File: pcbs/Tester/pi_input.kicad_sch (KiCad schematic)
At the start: 3 parts, among them J201 Raspberry_Pi_2_3, U201 SN74LVC4245APWR, U202 SN74LVC4245APWR

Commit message: More renaming
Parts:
- added U?: SN74LVC4245APWR, Package_SO:TSSOP-24_4.4x7.8mm_P0.65mm, symbol LevelShifter:SN74LVC4245APWR
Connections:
- net +3V3: now also U?.23 (VCCB), U?.24 (VCCB)
- net +5V: now also U?.1 (VCCA)
- net GND: now also U?.11 (GND), U?.12 (GND), U?.13 (GND), U?.14 (B8), U?.18 (B4), U?.2 (DIR), U?.22 (~{OE}); no longer U201.14 (B8), U201.18 (B4)
- net IN_{CLK}: now also U?.9 (A7); no longer U201.9 (A7)
- net SPI1_{CLK}: now also U?.15 (B7); no longer U201.15 (B7)
- net ~{IN_{LOAD}}: now also U?.8 (A6); no longer U201.8 (A6)
- net ~{IN_{SELECT}}: now also U?.7 (A5); no longer U201.7 (A5)
- net ~{SPI1_{LOAD}}: now also U?.16 (B6); no longer U201.16 (B6)
- net ~{SPI1_{SELECT}}: now also U?.17 (B5); no longer U201.17 (B5)
- net ~{OE5}: now reaches U201.10 (A8)
- net ~{OE1}: now reaches U201.6 (A4)
- new net ~{OE2}: U201.7 (A5)
- new net ~{OE3}: U201.8 (A6)
- new net ~{OE4}: U201.9 (A7)
- new net ~{SPI0_{OE1}}: U201.14 (B8), U201.15 (B7), U201.16 (B6), U201.17 (B5), U201.18 (B4)
- no-connect marks 30 -> 13
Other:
- moved on the sheet: U201, U202

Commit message: Lots of rethinking
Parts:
- gave numbers to parts that had none: 1
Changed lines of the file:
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@@
   (symbol (lib_id "power:GND") (at 276.225 66.04 90) (unit 1)
     (in_bom yes) (on_board yes) (fields_autoplaced)
-    (property "Reference" "#PWR?" (id 0) (at 282.575 66.04 0)
+    (property "Reference" "#PWR0222" (id 0) (at 282.575 66.04 0)
       (effects (font (size 1.27 1.27)) hide)
     )
@@
   (symbol (lib_id "power:+5V") (at 227.965 38.1 90) (unit 1)
     (in_bom yes) (on_board yes) (fields_autoplaced)
-    (property "Reference" "#PWR?" (id 0) (at 231.775 38.1 0)
+    (property "Reference" "#PWR0218" (id 0) (at 231.775 38.1 0)
       (effects (font (size 1.27 1.27)) hide)
     )
@@
   (symbol (lib_id "power:+3V3") (at 263.525 39.37 270) (unit 1)
     (in_bom yes) (on_board yes) (fields_autoplaced)
-    (property "Reference" "#PWR?" (id 0) (at 259.715 39.37 0)
+    (property "Reference" "#PWR0220" (id 0) (at 259.715 39.37 0)
       (effects (font (size 1.27 1.27)) hide)
     )
@@
   (symbol (lib_id "power:GND") (at 276.225 55.88 90) (unit 1)
     (in_bom yes) (on_board yes) (fields_autoplaced)
-    (property "Reference" "#PWR?" (id 0) (at 282.575 55.88 0)
+    (property "Reference" "#PWR0221" (id 0) (at 282.575 55.88 0)
       (effects (font (size 1.27 1.27)) hide)
     )
@@
   (symbol (lib_id "power:GND") (at 227.965 41.91 270) (unit 1)
     (in_bom yes) (on_board yes) (fields_autoplaced)
-    (property "Reference" "#PWR?" (id 0) (at 221.615 41.91 0)
+    (property "Reference" "#PWR0219" (id 0) (at 221.615 41.91 0)
       (effects (font (size 1.27 1.27)) hide)
     )
@@
   (symbol (lib_id "LevelShifter:SN74LVC4245APWR") (at 245.745 57.15 0) (unit 1)
     (in_bom yes) (on_board yes)
-    (property "Reference" "U?" (id 0) (at 245.745 29.083 0))
+    (property "Reference" "U203" (id 0) (at 245.745 29.083 0))
     (property "Value" "SN74LVC4245APWR" (id 1) (at 245.745 31.3944 0))
     (property "Footprint" "Package_SO:TSSOP-24_4.4x7.8mm_P0.65mm" (id 2) (at 245.745 57.15 0)
@@
   (symbol (lib_id "power:GND") (at 219.075 44.45 270) (unit 1)
     (in_bom yes) (on_board yes) (fields_autoplaced)
-    (property "Reference" "#PWR?" (id 0) (at 212.725 44.45 0)
+    (property "Reference" "#PWR0216" (id 0) (at 212.725 44.45 0)
       (effects (font (size 1.27 1.27)) hide)
     )
@@
   (symbol (lib_id "power:GND") (at 226.695 74.93 270) (unit 1)
     (in_bom yes) (on_board yes) (fields_autoplaced)
-    (property "Reference" "#PWR?" (id 0) (at 220.345 74.93 0)
-      (effects (font (size 1.27 1.27)) hide)
-    )
+    (property "Reference" "#PWR0217" (id 0) (at 220.345 74.93 0)
+      (effects (font (size 1.27 1.27)) hide)
+    )

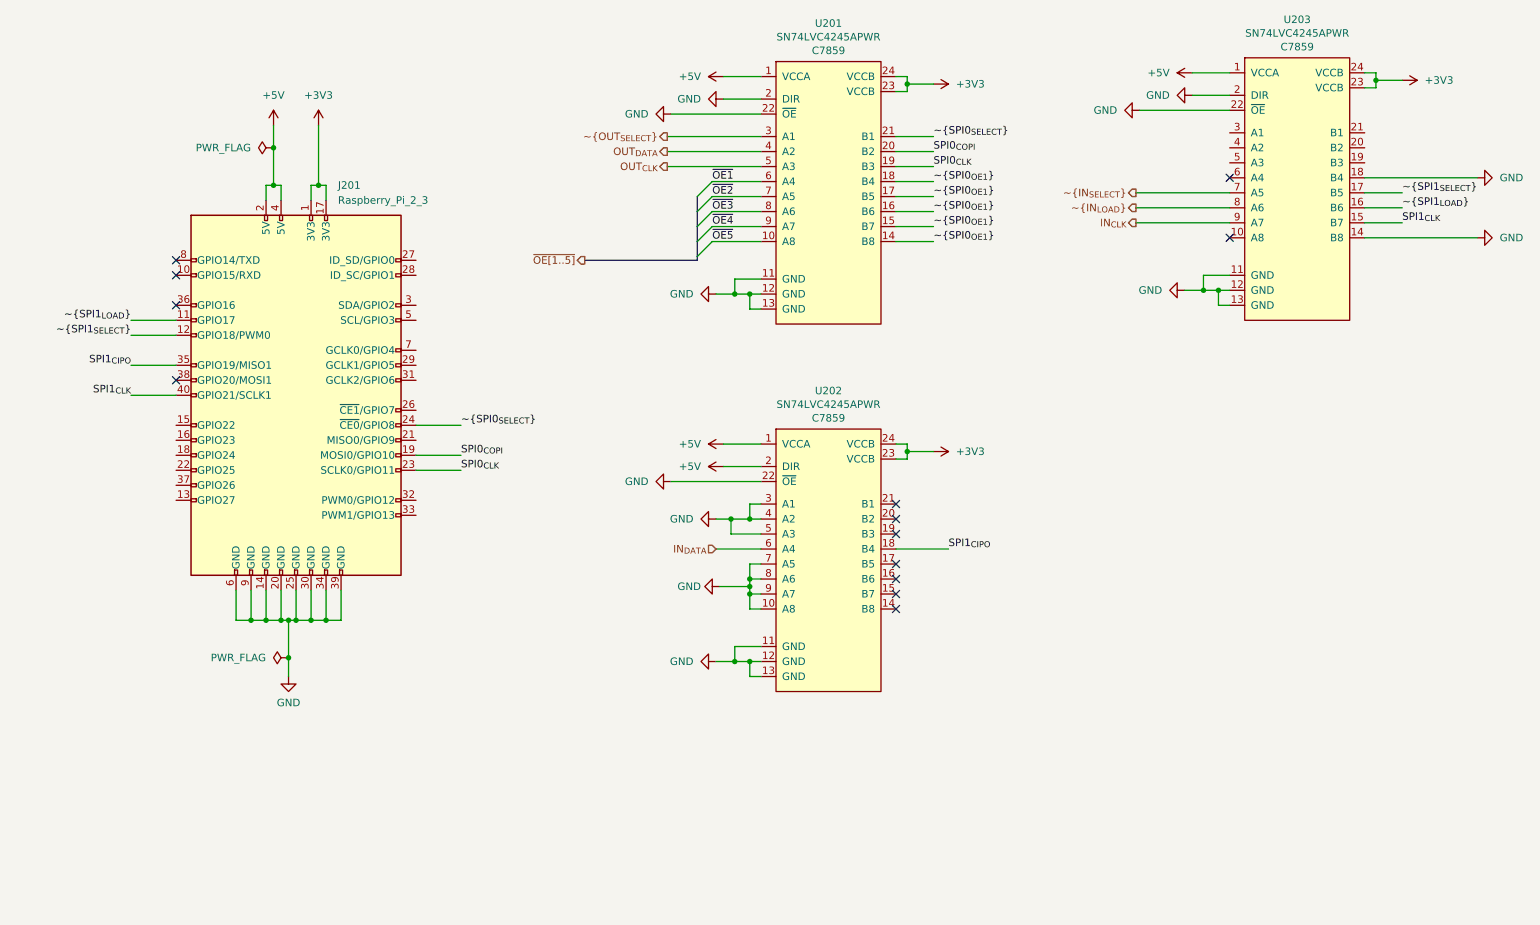
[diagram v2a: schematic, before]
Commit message: Shift register routing
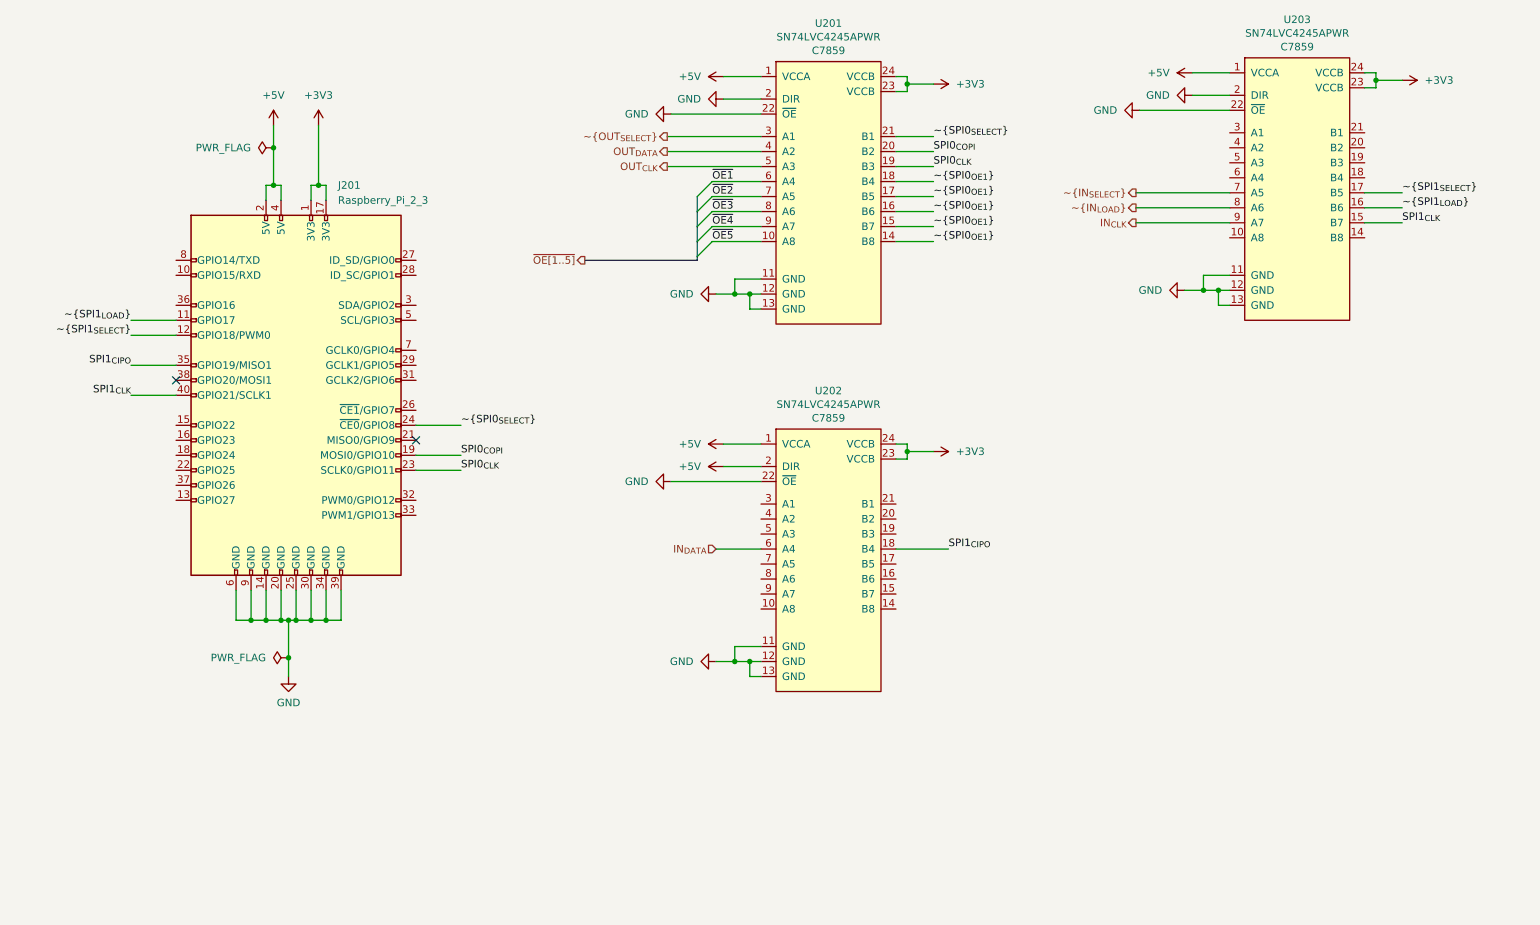
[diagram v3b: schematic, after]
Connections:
- net GND: no longer U202.10 (A8), U202.3 (A1), U202.4 (A2), U202.5 (A3), U202.7 (A5), U202.8 (A6), U202.9 (A7), U203.14 (B8), U203.18 (B4)
- no-connect marks 13 -> 2
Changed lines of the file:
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@@
   (junction (at 72.39 57.15) (diameter 0) (color 0 0 0 0)
   )
-  (junction (at 153.035 123.825) (diameter 0) (color 0 0 0 0)
-  )
   (junction (at 78.74 130.81) (diameter 0) (color 0 0 0 0)
   )
-  (junction (at 153.035 126.365) (diameter 0) (color 0 0 0 0)
-  )
   (junction (at 68.58 130.81) (diameter 0) (color 0 0 0 0)
   )
@@
   (junction (at 76.2 130.81) (diameter 0) (color 0 0 0 0)
   )
-  (junction (at 149.86 113.665) (diameter 0) (color 0 0 0 0)
-  )
-  (junction (at 153.035 125.095) (diameter 0) (color 0 0 0 0)
-  )
-  (junction (at 153.035 113.665) (diameter 0) (color 0 0 0 0)
-  )
   (junction (at 81.28 130.81) (diameter 0) (color 0 0 0 0)
   )
   (junction (at 179.705 102.235) (diameter 0) (color 0 0 0 0)
   )
-  (no_connect (at 177.8 126.365))
-  (no_connect (at 177.8 111.125))
-  (no_connect (at 177.8 123.825))
-  (no_connect (at 234.315 66.04))
-  (no_connect (at 177.8 113.665))
-  (no_connect (at 177.8 128.905))
-  (no_connect (at 177.8 121.285))
-  (no_connect (at 55.88 77.47))
+  (no_connect (at 96.52 100.33))
   (no_connect (at 55.88 90.17))
-  (no_connect (at 55.88 69.85))
-  (no_connect (at 55.88 72.39))
-  (no_connect (at 177.8 116.205))
-  (no_connect (at 234.315 55.88))
   (bus_entry (at 144.145 61.595) (size 2.54 -2.54)
     (stroke (width 0) (type default) (color 0 0 0 0))
@@
     (stroke (width 0) (type default) (color 0 0 0 0))
   )
-  (wire (pts (xy 154.94 128.905) (xy 153.035 128.905))
-    (stroke (width 0) (type default) (color 0 0 0 0))
-  )
   (wire (pts (xy 177.8 103.505) (xy 179.705 103.505))
     (stroke (width 0) (type default) (color 0 0 0 0))
@@
     (stroke (width 0) (type default) (color 0 0 0 0))
   )
-  (wire (pts (xy 257.175 55.88) (xy 276.225 55.88))
-    (stroke (width 0) (type default) (color 0 0 0 0))
-  )
-  (wire (pts (xy 154.94 116.205) (xy 149.86 116.205))
-    (stroke (width 0) (type default) (color 0 0 0 0))
-  )
-  (wire (pts (xy 147.32 113.665) (xy 149.86 113.665))
-    (stroke (width 0) (type default) (color 0 0 0 0))
-  )
   (wire (pts (xy 154.94 140.335) (xy 153.035 140.335))
     (stroke (width 0) (type default) (color 0 0 0 0))
@@
     (stroke (width 0) (type default) (color 0 0 0 0))
   )
-  (wire (pts (xy 153.035 113.665) (xy 154.94 113.665))
-    (stroke (width 0) (type default) (color 0 0 0 0))
-  )
   (wire (pts (xy 153.035 137.795) (xy 154.94 137.795))
     (stroke (width 0) (type default) (color 0 0 0 0))
@@
     (stroke (width 0) (type default) (color 0 0 0 0))
   )
-  (wire (pts (xy 153.035 128.905) (xy 153.035 126.365))
-    (stroke (width 0) (type default) (color 0 0 0 0))
-  )
   (wire (pts (xy 71.12 59.69) (xy 71.12 57.15))
     (stroke (width 0) (type default) (color 0 0 0 0))
@@
     (stroke (width 0) (type default) (color 0 0 0 0))
   )
-  (wire (pts (xy 153.035 126.365) (xy 154.94 126.365))
-    (stroke (width 0) (type default) (color 0 0 0 0))
-  )
   (wire (pts (xy 177.8 118.745) (xy 186.69 118.745))
     (stroke (width 0) (type default) (color 0 0 0 0))
@@
     (stroke (width 0) (type default) (color 0 0 0 0))
   )
-  (wire (pts (xy 153.035 123.825) (xy 153.035 125.095))
-    (stroke (width 0) (type default) (color 0 0 0 0))
-  )
   (wire (pts (xy 96.52 102.87) (xy 104.14 102.87))
     (stroke (width 0) (type default) (color 0 0 0 0))
   )
-  (wire (pts (xy 153.035 125.095) (xy 153.035 126.365))
-    (stroke (width 0) (type default) (color 0 0 0 0))
-  )
   (wire (pts (xy 96.52 105.41) (xy 104.14 105.41))
     (stroke (width 0) (type default) (color 0 0 0 0))
@@
     (stroke (width 0) (type default) (color 0 0 0 0))
   )
-  (wire (pts (xy 147.955 125.095) (xy 153.035 125.095))
-    (stroke (width 0) (type default) (color 0 0 0 0))
-  )
   (wire (pts (xy 227.965 41.91) (xy 234.315 41.91))
     (stroke (width 0) (type default) (color 0 0 0 0))
   )
-  (wire (pts (xy 257.175 66.04) (xy 276.225 66.04))
-    (stroke (width 0) (type default) (color 0 0 0 0))
-  )
   (wire (pts (xy 179.705 38.735) (xy 179.705 40.005))
     (stroke (width 0) (type default) (color 0 0 0 0))
   )
-  (wire (pts (xy 153.035 121.285) (xy 154.94 121.285))
-    (stroke (width 0) (type default) (color 0 0 0 0))
-  )
   (wire (pts (xy 234.315 77.47) (xy 232.41 77.47))
     (stroke (width 0) (type default) (color 0 0 0 0))
@@
     (stroke (width 0) (type default) (color 0 0 0 0))
   )
-  (wire (pts (xy 153.035 111.125) (xy 153.035 113.665))
-    (stroke (width 0) (type default) (color 0 0 0 0))
-  )
   (wire (pts (xy 218.44 60.96) (xy 234.315 60.96))
     (stroke (width 0) (type default) (color 0 0 0 0))
   )
-  (wire (pts (xy 149.86 113.665) (xy 153.035 113.665))
-    (stroke (width 0) (type default) (color 0 0 0 0))
-  )
   (wire (pts (xy 257.175 40.64) (xy 259.08 40.64))
     (stroke (width 0) (type default) (color 0 0 0 0))
@@
     (stroke (width 0) (type default) (color 0 0 0 0))
   )
-  (wire (pts (xy 149.86 116.205) (xy 149.86 113.665))
-    (stroke (width 0) (type default) (color 0 0 0 0))
-  )
-  (wire (pts (xy 154.94 111.125) (xy 153.035 111.125))
-    (stroke (width 0) (type default) (color 0 0 0 0))
-  )
   (wire (pts (xy 73.66 130.81) (xy 74.93 130.81))
     (stroke (width 0) (type default) (color 0 0 0 0))
@@
     (stroke (width 0) (type default) (color 0 0 0 0))
   )
-  (wire (pts (xy 154.94 123.825) (xy 153.035 123.825))
-    (stroke (width 0) (type default) (color 0 0 0 0))
-  )
   (wire (pts (xy 154.94 73.025) (xy 150.495 73.025))
     (stroke (width 0) (type default) (color 0 0 0 0))
@@
   )
   (wire (pts (xy 257.175 60.96) (xy 263.525 60.96))
-    (stroke (width 0) (type default) (color 0 0 0 0))
-  )
-  (wire (pts (xy 153.035 123.825) (xy 153.035 121.285))
     (stroke (width 0) (type default) (color 0 0 0 0))
   )
@@
   (hierarchical_label "~{IN_{LOAD}}" (shape output) (at 218.44 60.96 180)
     (effects (font (size 1.27 1.27)) (justify right))
-  )
-  (symbol (lib_id "power:GND") (at 276.225 66.04 90) (unit 1)
-    (in_bom yes) (on_board yes) (fields_autoplaced)
-    (property "Reference" "#PWR0222" (id 0) (at 282.575 66.04 0)
-      (effects (font (size 1.27 1.27)) hide)
-    )
-    (property "Value" "GND" (id 1) (at 280.035 66.0399 90)
-      (effects (font (size 1.27 1.27)) (justify right))
-    )
-    (property "Footprint" "" (id 2) (at 276.225 66.04 0)
-      (effects (font (size 1.27 1.27)) hide)
-    )
-    (property "Datasheet" "" (id 3) (at 276.225 66.04 0)
-      (effects (font (size 1.27 1.27)) hide)
-    )
-    (pin "1")
   )
   (symbol (lib_id "power:+5V") (at 227.965 38.1 90) (unit 1)
@@
     )
     (property "Datasheet" "~" (id 3) (at 72.39 50.8 0)
-      (effects (font (size 1.27 1.27)) hide)
-    )
-    (pin "1")
-  )
-  (symbol (lib_id "power:GND") (at 276.225 55.88 90) (unit 1)
-    (in_bom yes) (on_board yes) (fields_autoplaced)
-    (property "Reference" "#PWR0221" (id 0) (at 282.575 55.88 0)
-      (effects (font (size 1.27 1.27)) hide)
-    )
-    (property "Value" "GND" (id 1) (at 280.035 55.8799 90)
-      (effects (font (size 1.27 1.27)) (justify right))
-    )
-    (property "Footprint" "" (id 2) (at 276.225 55.88 0)
-      (effects (font (size 1.27 1.27)) hide)
-    )
-    (property "Datasheet" "" (id 3) (at 276.225 55.88 0)
       (effects (font (size 1.27 1.27)) hide)
     )
@@
     (pin "9")
   )
-  (symbol (lib_id "power:GND") (at 147.955 125.095 270) (unit 1)
-    (in_bom yes) (on_board yes) (fields_autoplaced)
-    (property "Reference" "#PWR0209" (id 0) (at 141.605 125.095 0)
-      (effects (font (size 1.27 1.27)) hide)
-    )
-    (property "Value" "GND" (id 1) (at 144.78 125.0949 90)
-      (effects (font (size 1.27 1.27)) (justify right))
-    )
-    (property "Footprint" "" (id 2) (at 147.955 125.095 0)
-      (effects (font (size 1.27 1.27)) hide)
-    )
-    (property "Datasheet" "" (id 3) (at 147.955 125.095 0)
-      (effects (font (size 1.27 1.27)) hide)
-    )
-    (pin "1")
-  )
   (symbol (lib_id "power:+5V") (at 148.59 100.965 90) (unit 1)
     (in_bom yes) (on_board yes) (fields_autoplaced)
@@
     (pin "9")
   )
-  (symbol (lib_id "power:GND") (at 147.32 113.665 270) (unit 1)
-    (in_bom yes) (on_board yes) (fields_autoplaced)
-    (property "Reference" "#PWR0207" (id 0) (at 140.97 113.665 0)
-      (effects (font (size 1.27 1.27)) hide)
-    )
-    (property "Value" "GND" (id 1) (at 143.51 113.6649 90)
-      (effects (font (size 1.27 1.27)) (justify right))
-    )
-    (property "Footprint" "" (id 2) (at 147.32 113.665 0)
-      (effects (font (size 1.27 1.27)) hide)
-    )
-    (property "Datasheet" "" (id 3) (at 147.32 113.665 0)
-      (effects (font (size 1.27 1.27)) hide)
-    )
-    (pin "1")
-  )
   (symbol (lib_id "power:GND") (at 147.32 75.565 270) (unit 1)

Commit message: Turn those transceivers the other way up
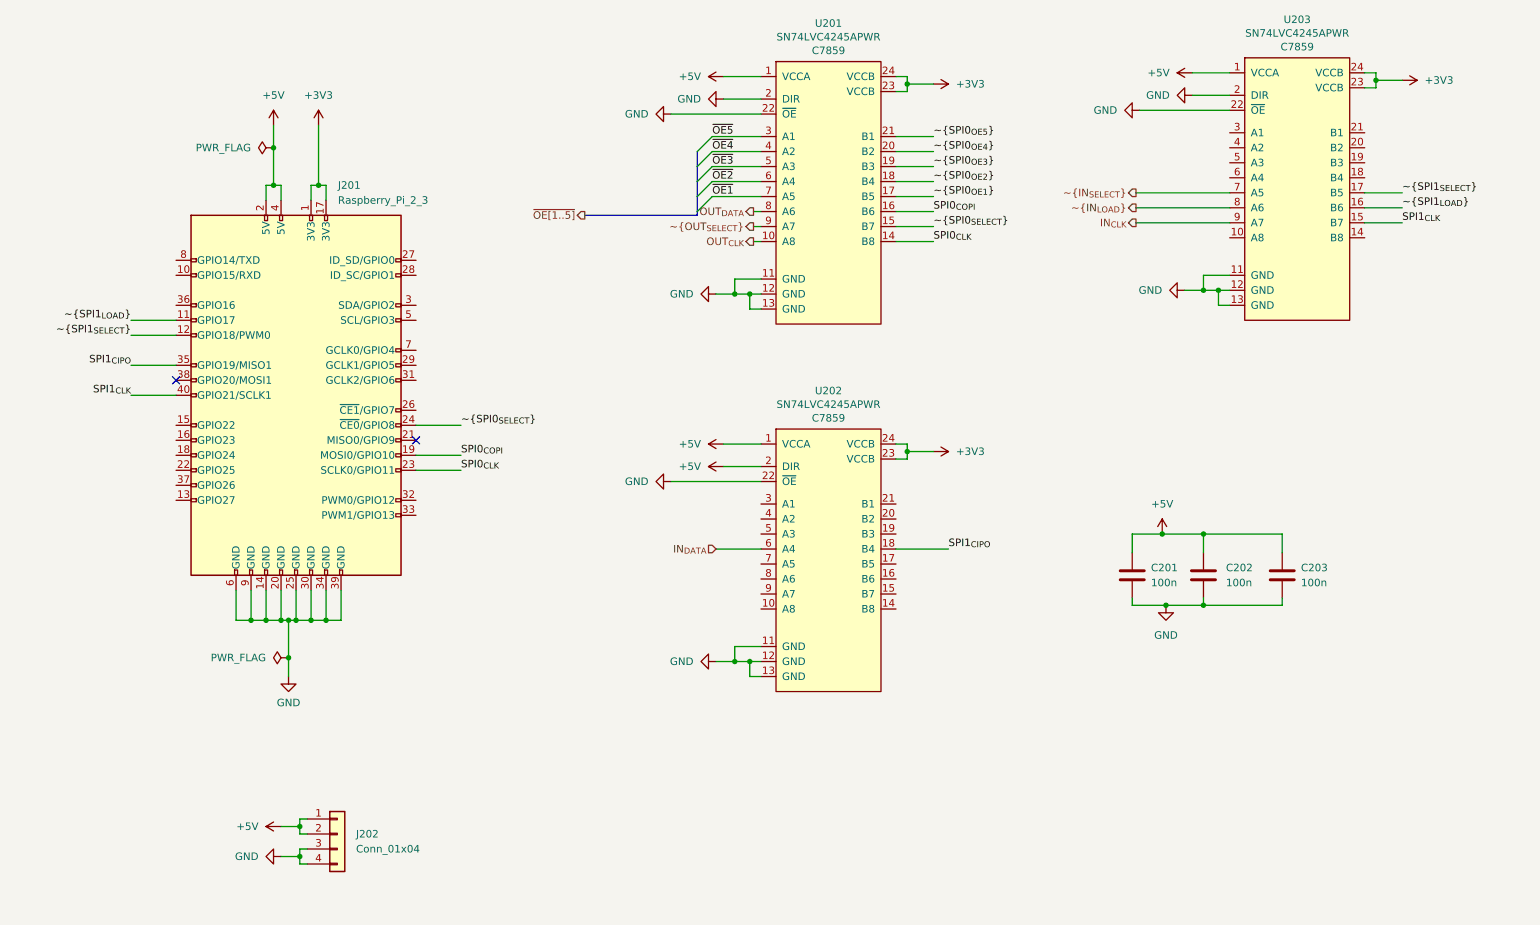
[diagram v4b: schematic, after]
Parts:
- added C201, C202, C203: 100n, Capacitor_SMD:C_0603_1608Metric, symbol Device:C
- added J202: Conn_01x04, symbol Connector_Generic:Conn_01x04
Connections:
- net +5V: now also C201.1, C202.1, C203.1, J202.1 (Pin_1), J202.2 (Pin_2)
- net GND: now also C201.2, C202.2, C203.2, J202.3 (Pin_3), J202.4 (Pin_4)
- net OUT_{CLK}: now also U201.10 (A8); no longer U201.5 (A3)
- net OUT_{DATA}: now also U201.8 (A6); no longer U201.4 (A2)
- net SPI0_{CLK}: now also U201.14 (B8); no longer U201.19 (B3)
- net SPI0_{COPI}: now also U201.16 (B6); no longer U201.20 (B2)
- net ~{OE1}: now also U201.7 (A5); no longer U201.6 (A4)
- net ~{OE2}: now also U201.6 (A4); no longer U201.7 (A5)
- net ~{OE3}: now also U201.5 (A3); no longer U201.8 (A6)
- net ~{OE4}: now also U201.4 (A2); no longer U201.9 (A7)
- net ~{OE5}: now also U201.3 (A1); no longer U201.10 (A8)
- net ~{OUT_{SELECT}}: now also U201.9 (A7); no longer U201.3 (A1)
- net ~{SPI0_{OE1}}: no longer U201.14 (B8), U201.15 (B7), U201.16 (B6), U201.18 (B4)
- net ~{SPI0_{SELECT}}: now also U201.15 (B7); no longer U201.21 (B1)
- new net ~{SPI0_{OE2}}: U201.18 (B4)
- new net ~{SPI0_{OE3}}: U201.19 (B3)
- new net ~{SPI0_{OE4}}: U201.20 (B2)
- new net ~{SPI0_{OE5}}: U201.21 (B1)
